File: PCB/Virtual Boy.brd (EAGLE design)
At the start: 58.5 x 61 mm, 12 parts, among them U1 SN74AHCT125N, U2 SN74AHCT125N

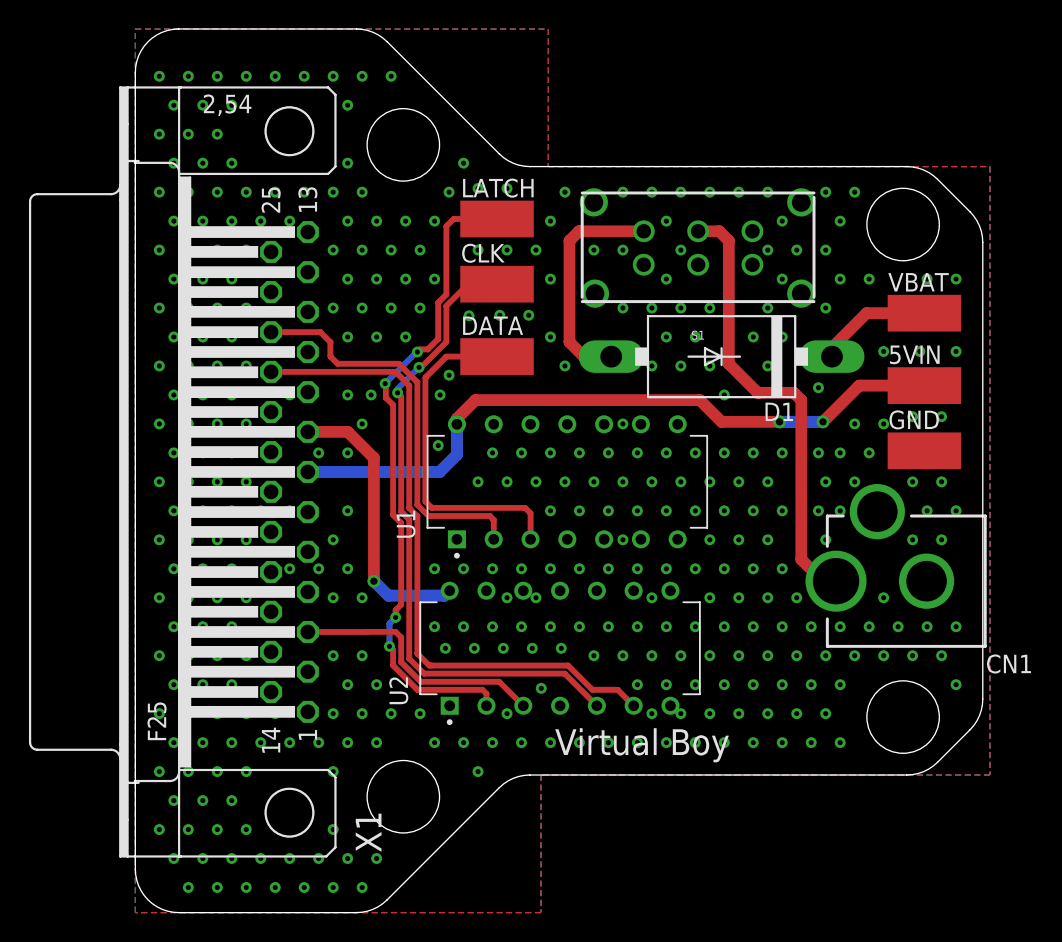
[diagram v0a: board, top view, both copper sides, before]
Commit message: Added exposed GND plane at DB25 anchors
All PCBs have been update to have exposed GND plane pads for the DB25 anchor points.

This resolves Issue 54
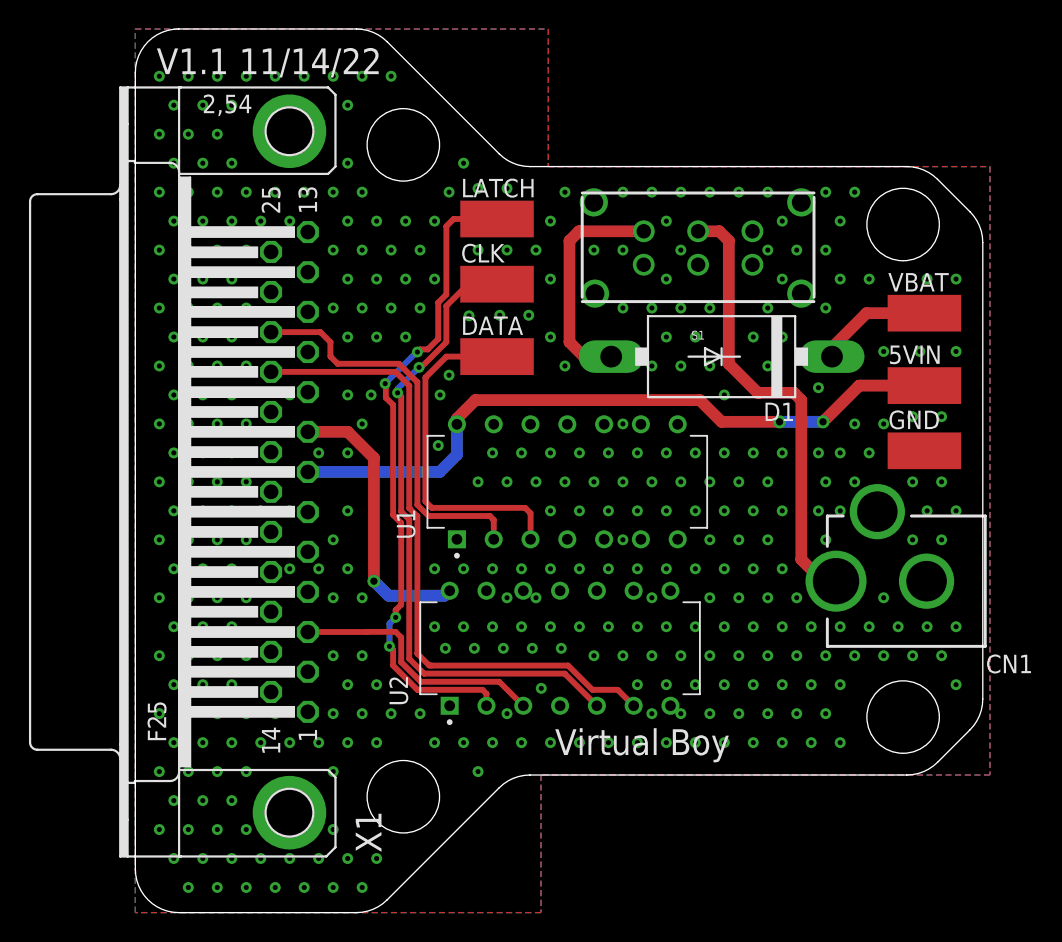
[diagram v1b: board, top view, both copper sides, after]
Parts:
- X1: device SparkFun-Retired:F25H -> SparkFun-Retired:F25HP
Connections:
- net GND: now also X1.GND1, X1.GND2
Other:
- board text added: "V1.1 11/14/22"
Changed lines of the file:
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@@
 <hole x="18.53" y="8.12" drill="5"/>
 <text x="29" y="11" size="1.778" layer="21">Virtual Boy</text>
+<text x="1.5" y="58" size="1.778" layer="25">V1.1 11/14/22</text>
 </plain>
 <attributes>
@@
 <attribute name="VALUE" x="40.35" y="25.86" size="1.27" layer="27" rot="R90" align="top-left"/>
 </element>
-<element name="X1" library="SparkFun-Retired" package="F25H" value="" x="10.67" y="30.54" smashed="yes" rot="R90">
+<element name="X1" library="SparkFun-Retired" package="F25HP" value="" x="10.67" y="30.54" smashed="yes" rot="R90">
 <attribute name="NAME" x="17.02" y="4.251" size="1.778" layer="25" ratio="10" rot="R90"/>
 <attribute name="VALUE" x="-3.3" y="22.158" size="1.778" layer="27" ratio="10" rot="R90"/>
@@
 <via x="56.6868" y="27.855840625" extent="1-16" drill="0.35"/>
 <via x="56.6868" y="43.855840625" extent="1-16" drill="0.35"/>
+<contactref element="X1" pad="GND1"/>
+<contactref element="X1" pad="GND2"/>
 </signal>
 <signal name="5VIN">

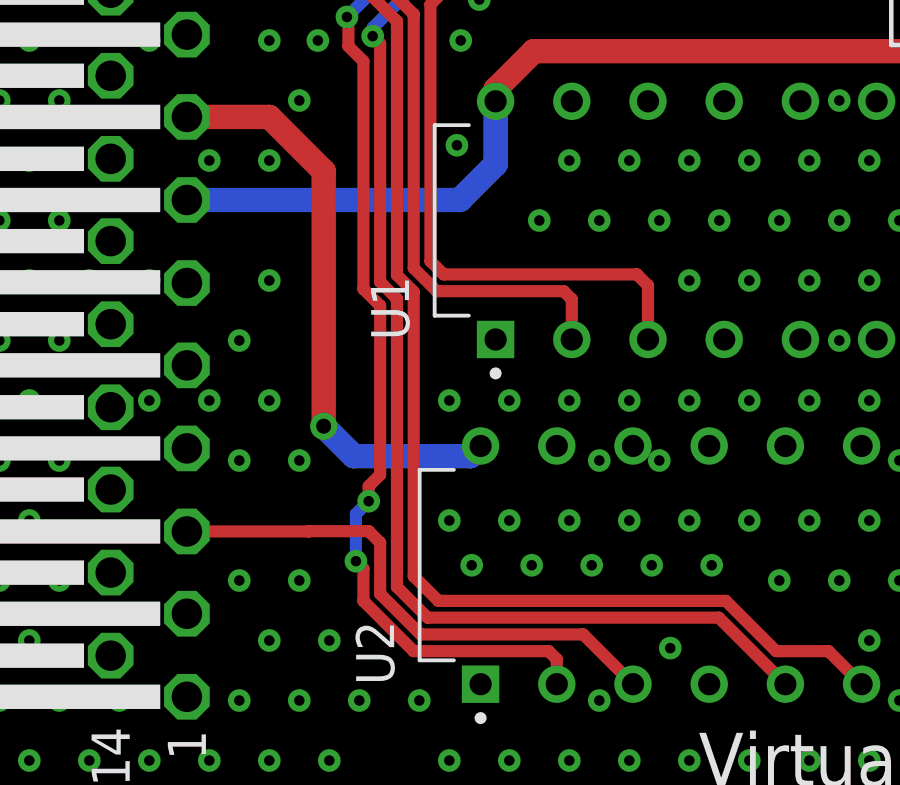
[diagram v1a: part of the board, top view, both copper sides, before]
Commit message: Silkscreen Update, Library Add, Datasheet Add
Updated the silkscreen on all PCBs that used the SN74 components as there was not orientation marker on the silkscreen.

Added Modified SN74 libraries and VB Cable Pinout image
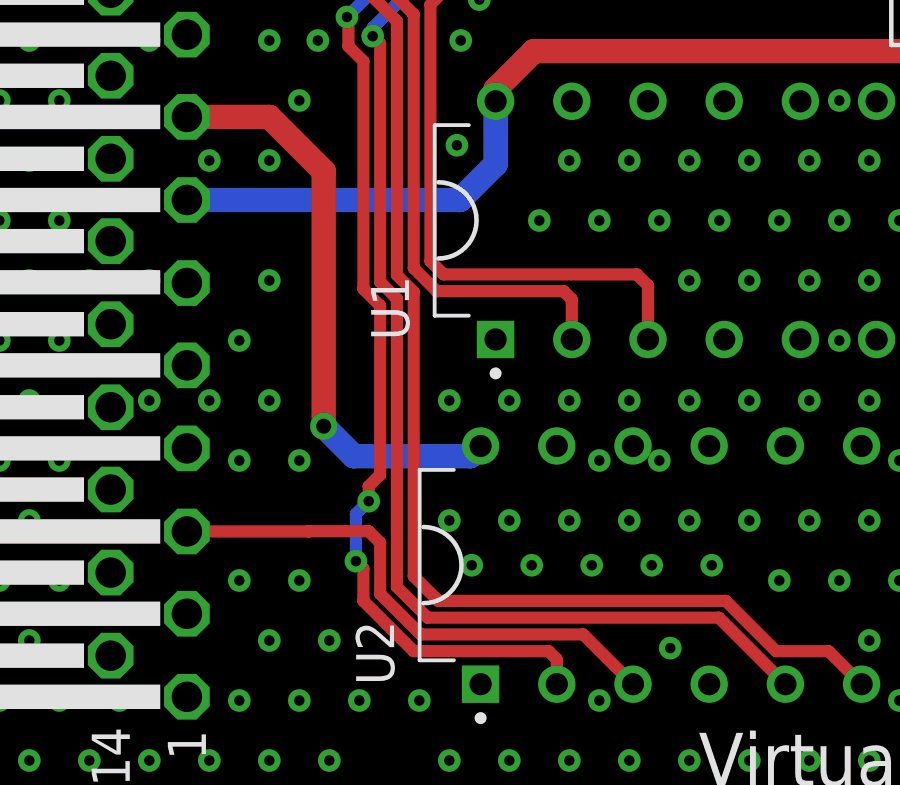
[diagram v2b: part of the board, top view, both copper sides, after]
